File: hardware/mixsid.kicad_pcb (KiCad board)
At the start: 2 copper layers, 61 x 55.9 mm, 71 parts, among them P1 INPUT, P2 CONTROL, P3 RAW, P4 SOCKET LEFT, P5 OUTPUT, P6 SOCKET RIGHT, P7 -5V, Q1 BC547, Q2 BC547, U1 GAL16V8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

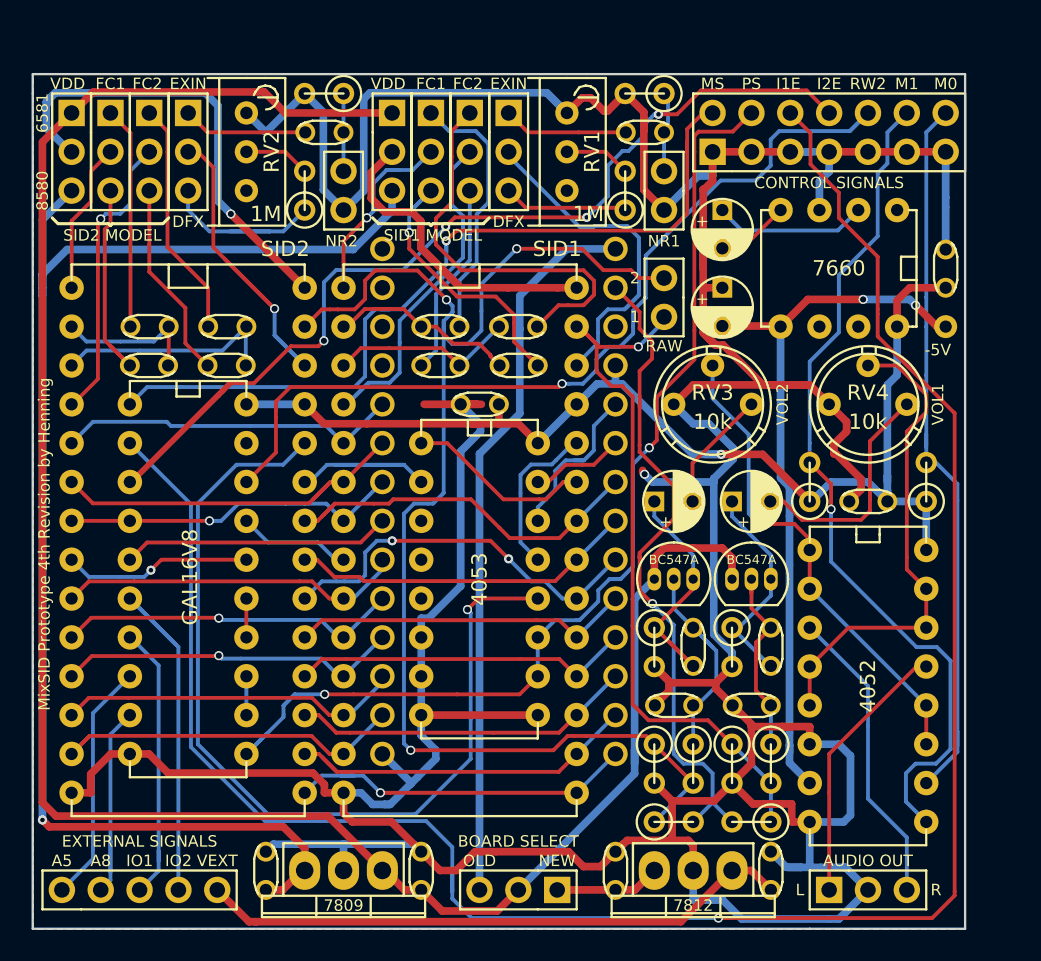
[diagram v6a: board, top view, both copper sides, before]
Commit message: Hardware: Added R8 Jumpers, Feed SID specific VDD into output stages
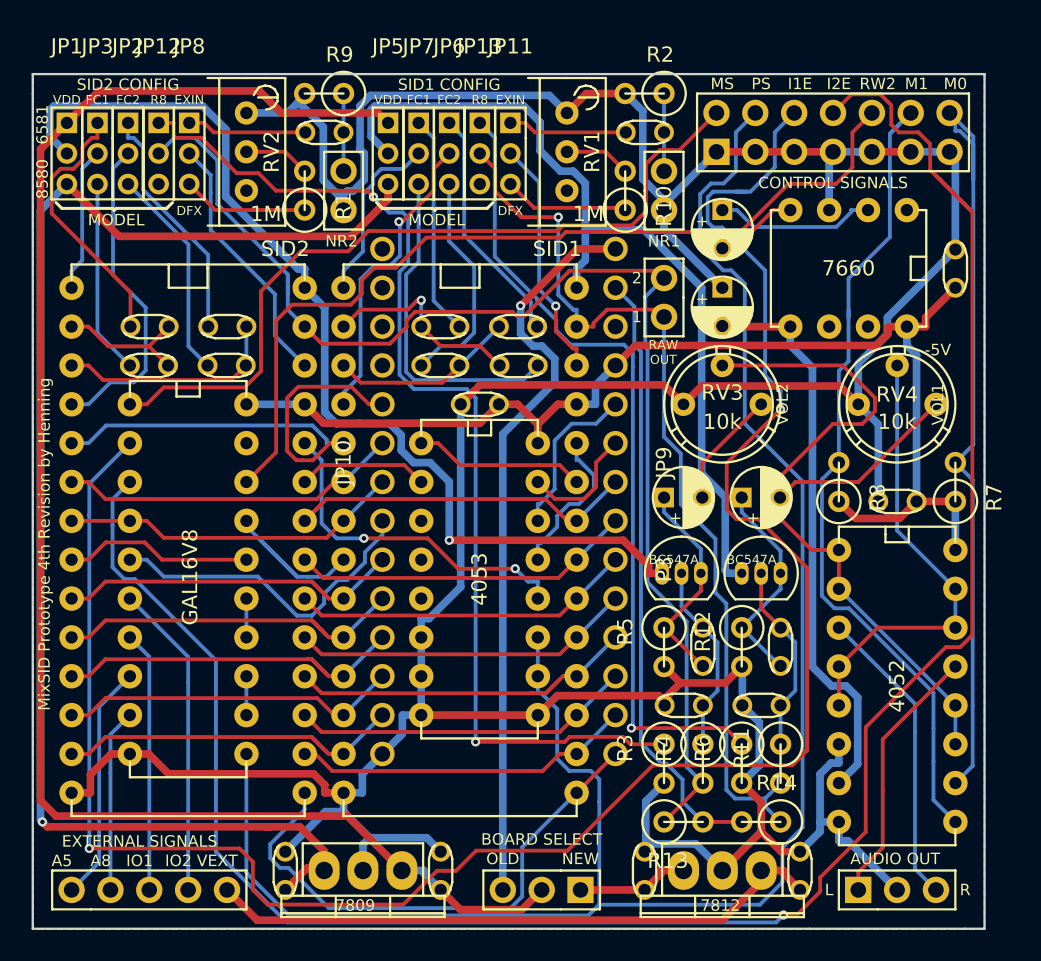
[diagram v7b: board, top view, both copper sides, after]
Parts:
- removed P7: -5V, Measurement_Points:Measurement_Point_Round-TH_Small
- added JP12: J2R8, Pinheaders:Pin_Header_Straight_1x03_Pitch2.00mm, F.Cu at (136.5, 70.5)
- added JP13: J1R8, Pinheaders:Pin_Header_Straight_1x03_Pitch2.00mm, F.Cu at (157.5, 70.5)
- JP1, JP11, JP2, JP3, JP5, JP6, JP7, JP8: footprint Pinheaders:Pin_Header_Straight_1x03 -> Pinheaders:Pin_Header_Straight_1x03_Pitch2.00mm
- R1, R10, R11, R12, R13, R14, R2, R3, R4, R5, R6, R7, R8, R9: footprint Pinheaders:R1 -> Discret:R1
- moved C25 1.91 mm to (186.1, 95.2)
- moved C5 1.91 mm to (178.4, 120.7)
- moved C6 1.91 mm to (168.3, 120.7)
- moved P5 1.91 mm to (182.2, 120.7)
- moved R7 1.91 mm to (188.6, 94.0)
- moved R8 1.91 mm to (181.0, 94.0)
- moved RV4 1.91 mm to (182.2, 88.9)
- moved U3 1.91 mm to (173.4, 119.4)
- moved U6 1.91 mm to (181.0, 98.4)
- moved JP2 1.53 mm to (134.5, 70.5)
- moved JP4 1.52 mm to (164.1, 120.7)
- moved JP6 1.49 mm to (155.5, 70.5)
- moved C7 1.27 mm to (154.9, 120.7)
- moved C8 1.27 mm to (144.8, 120.7)
- moved U4 1.27 mm to (149.9, 119.4)
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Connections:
- Q1 pad 1: /+12V -> /PWR2
- Q2 pad 1: /+12V -> /PWR1
- R3 pad 1: /S2OUT -> Net-(JP12-Pad1)
- R6 pad 1: /S1OUT -> Net-(JP13-Pad1)
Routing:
- net GND: track 343.1 -> 270.5 mm, vias 1 -> 0
- net Net-(JP12-Pad1): track 0.00 -> 70.6 mm, vias 0 -> 2
- net /~IO2EN: track 70.0 -> 137.2 mm, vias 4 -> 1
- net Net-(JP13-Pad1): track 0.00 -> 53.5 mm, vias 0 -> 1
- net /PS: track 70.2 -> 120.9 mm, vias 2 -> 0
- net /POTX2: track 60.8 -> 22.5 mm, vias 1 -> 2
- net /PWR2: track 31.4 -> 66.5 mm
- net /+12V: track 138.4 -> 104.2 mm
- net /PWR1: track 23.8 -> 57.1 mm
- net /S1OUT: track 47.7 -> 60.8 mm
- net /D0: track 23.2 -> 35.2 mm, vias 1 -> 0
- net /LEFT: track 32.0 -> 43.8 mm, vias 1 -> 0
- net /~RES: track 22.5 -> 33.8 mm
- net Net-(C9-Pad2): track 26.3 -> 15.7 mm
- net /S1IN: track 26.1 -> 15.8 mm, vias 0 -> 1
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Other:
- board size 61 x 55.9 mm -> 62.2 x 55.9 mm
- net class Default: clearance 0.2 -> 0.18
- net class Power: clearance 0.2 -> 0.18
- rule trace_clearance: 0.2 -> 0.18
- board text added: "MODEL"
- board text added: "R8"
- board text added: "RAW OUT"
- board text added: "SID1 CONFIG"
- board text added: "SID2 CONFIG"
- board text removed: "RAW"
- board text removed: "SID1 MODEL"
- board text removed: "SID2 MODEL"

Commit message: Hardware: Reverted to +12V for both output stages, rerouted, refined
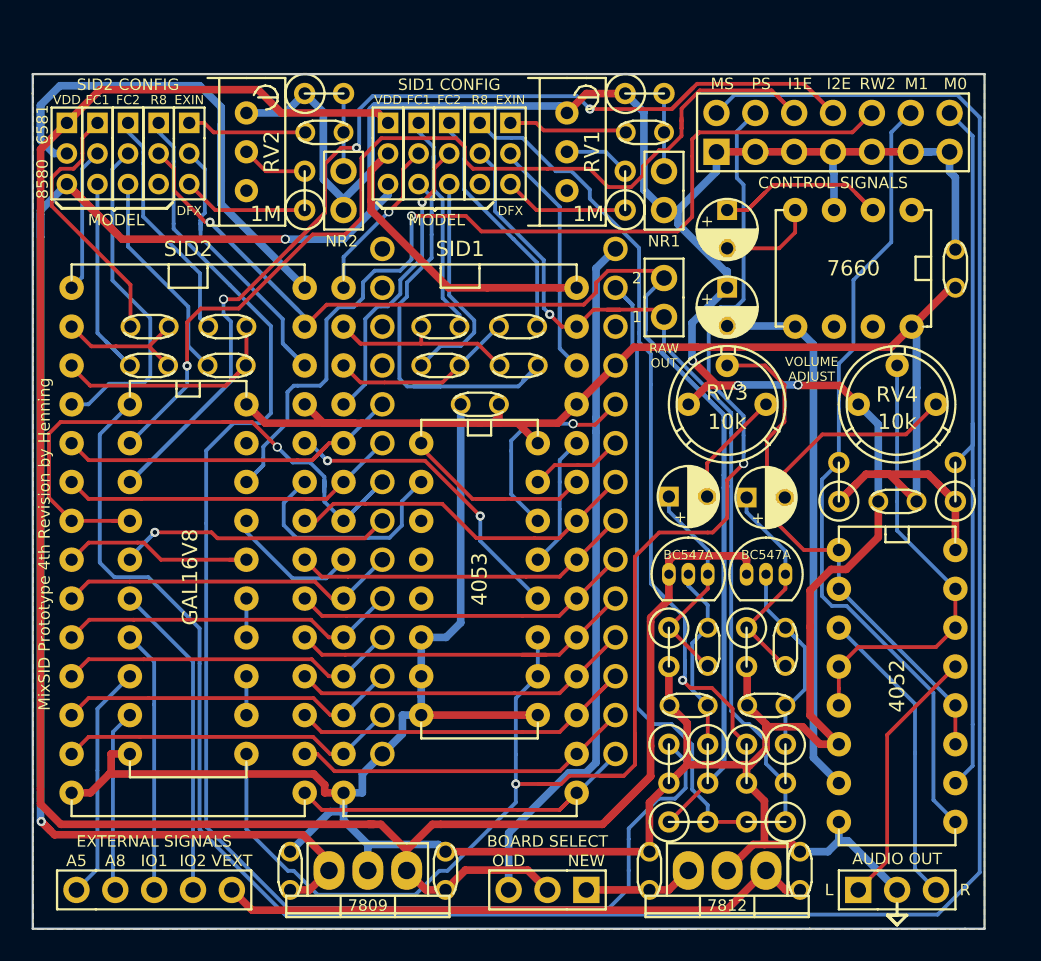
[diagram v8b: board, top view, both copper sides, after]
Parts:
- R1, R10, R11, R12, R13, R14, R2, R3, R4, R5, R6, R7, R8, R9: footprint Discret:R1 -> Pinheaders:R1
- moved Q1 0.45 mm to (169.9, 100.0)
- moved JP4 0.38 mm to (164.5, 120.7)
- moved C19 0.32 mm to (169.9, 94.9)
- moved Q2 0.32 mm to (174.9, 100.0)
- moved C7 0.32 mm to (155.3, 120.7)
- moved C8 0.32 mm to (145.1, 120.7)
- moved U8 0.32 mm to (185.7, 76.2)
- moved P1 0.32 mm to (131.1, 120.7)
- moved U4 0.32 mm to (150.2, 119.4)
- moved C17 0.32 mm to (173.7, 76.2)
- moved C18 0.32 mm to (173.7, 81.3)
- moved C20 0.32 mm to (177.5, 108.6)
- moved C21 0.32 mm to (177.5, 103.5)
- moved C22 0.32 mm to (174.9, 95.0)
- moved C6 0.32 mm to (168.6, 120.7)
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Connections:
- Q1 pad 1: /PWR2 -> /+12V
- Q2 pad 1: /PWR1 -> /+12V
- R2 pad 1: Net-(C14-Pad1) -> GND
- R2 pad 2: GND -> Net-(C14-Pad1)
- R9 pad 1: Net-(C13-Pad1) -> GND
- R9 pad 2: GND -> Net-(C13-Pad1)
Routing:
- net /MS: track 51.5 -> 154.7 mm
- net /~IO1EN: track 134.3 -> 65.3 mm, vias 2 -> 1
- net /~IO2EN: track 137.2 -> 81.6 mm, vias 1 -> 3
- net /+12V: track 104.2 -> 150.9 mm
- net /S2OUT: track 84.6 -> 128.9 mm, vias 0 -> 1
- net /PWR1: track 57.1 -> 19.7 mm
- net /PWR2: track 66.5 -> 38.2 mm, vias 1 -> 0
- net Net-(JP12-Pad1): track 70.6 -> 94.6 mm, vias 2 -> 0
- net /RW: track 22.3 -> 43.6 mm, vias 0 -> 1
- net /PS: track 120.9 -> 101.6 mm, vias 0 -> 2
- net VCC: track 77.6 -> 90.8 mm
- net /D0: track 35.2 -> 24.4 mm
- net /~RES: track 33.8 -> 23.6 mm
- net /+9V: track 90.7 -> 99.2 mm, vias 1 -> 2
- net /LEFT: track 43.8 -> 35.5 mm
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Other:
- board text added: "VOLUME ADJUST"
- board text removed: "-5V"
- board text removed: "VOL1"
- board text removed: "VOL2"
